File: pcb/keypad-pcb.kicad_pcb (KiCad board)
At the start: 2 copper layers, 38.1 x 59.9 mm, 20 parts, among them SW1 SW_Push, U1 ATmega32U4-A, Y1 Crystal_GND24_Small

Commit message: finalized pcb and created gerbers
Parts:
- moved R3 3.49 mm to (71.1, 88.4)
- moved USB1 3.49 mm to (59.5, 86.6)
- moved R2 2.86 mm to (71.1, 86.0)
- moved SW1 2.73 mm to (88.6, 88.6)
- moved F1 2.20 mm to (76.3, 92.1)
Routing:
- net GND: track 137.9 -> 131.7 mm
- net Net-(U1-D+): track 20.9 -> 16.5 mm
- net +5V: track 119.9 -> 123.2 mm, vias 4 -> 5
- net Net-(U1-D-): track 22.2 -> 19.2 mm
- net VCC: track 11.4 -> 12.5 mm
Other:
- board size 38.1 x 59.9 mm -> 38.1 x 56.3 mm

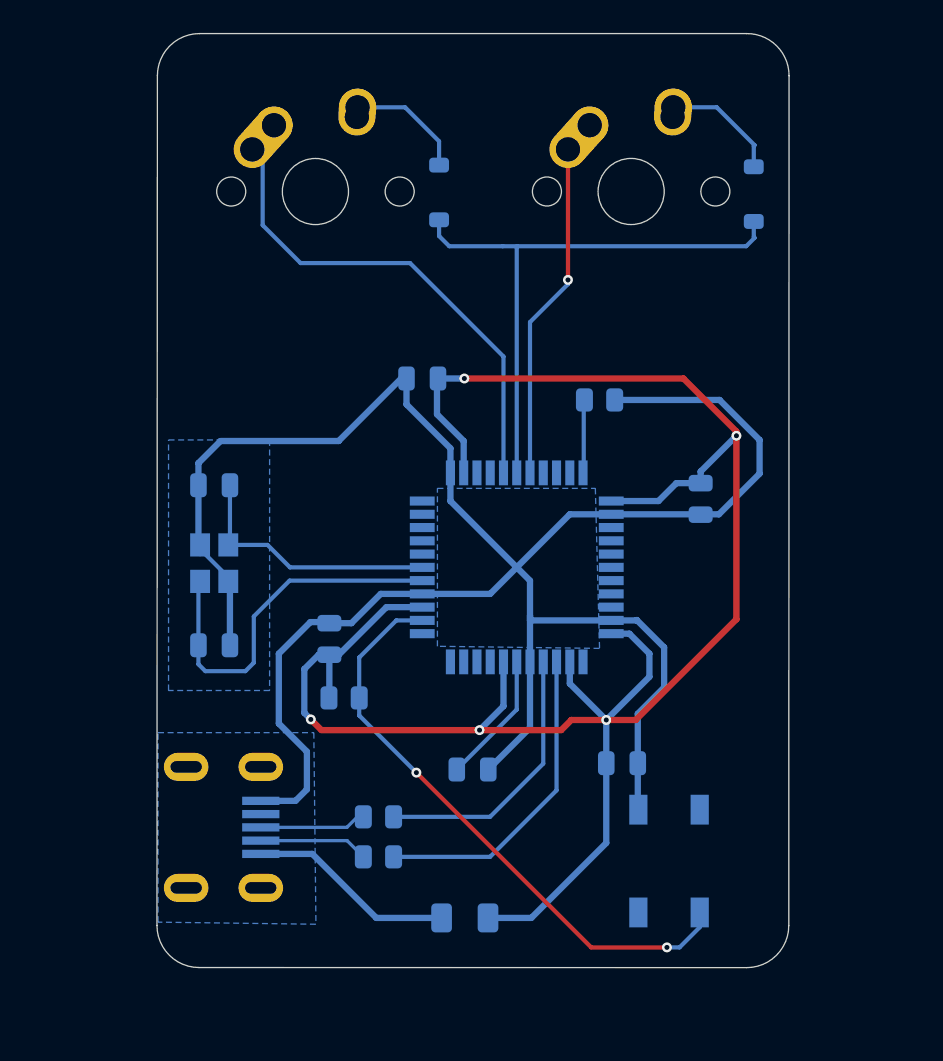
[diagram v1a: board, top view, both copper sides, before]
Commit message: redesigned pcb for front-facing usb
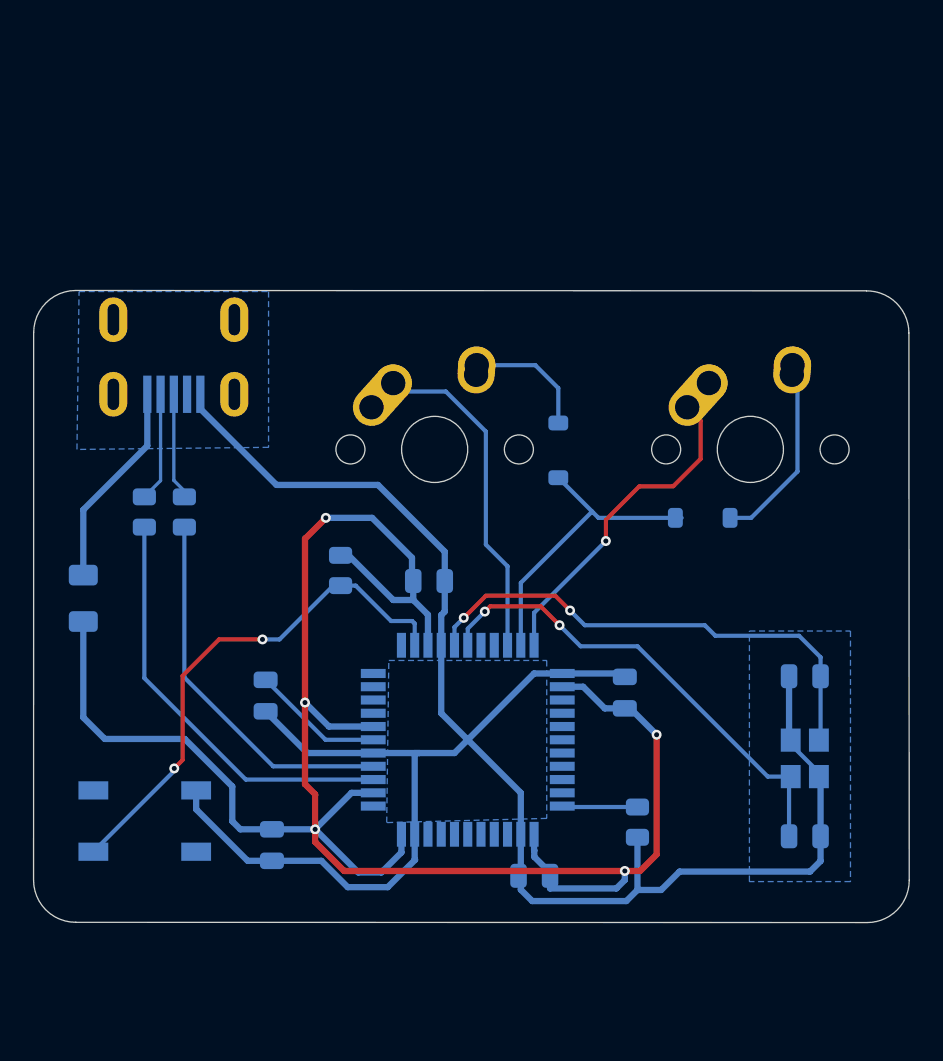
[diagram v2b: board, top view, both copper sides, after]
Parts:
- moved C6 41.4 mm to (96.8, 87.2), turned to 180 degrees
- moved Y1 37.5 mm to (96.8, 82.5), turned to 90 degrees
- moved C7 35.7 mm to (96.8, 77.5), turned to 0 degrees
- moved SW1 31.7 mm to (57.0, 86.2), turned to 0 degrees
- moved USB1 30.6 mm to (58.8, 56.0), turned to -90 degrees
- moved F1 30.0 mm to (53.3, 72.8), turned to -90 degrees
- moved R1 25.6 mm to (86.7, 86.3), turned to -90 degrees
- moved R3 25.1 mm to (57.0, 67.6), turned to -90 degrees
- moved C4 24.8 mm to (80.5, 89.5), turned to 180 degrees
- moved C3 22.5 mm to (86.0, 78.5), turned to 90 degrees
- moved R2 21.8 mm to (59.4, 67.6), turned to 90 degrees
- moved C5 21.7 mm to (64.7, 87.7), turned to -90 degrees
- moved D2 19.8 mm to (90.7, 67.9), turned to 0 degrees
- moved MX1 17.1 mm to (74.5, 63.8)
- moved MX2 17.1 mm to (93.6, 63.8)
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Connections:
- U1 pad 20: unconnected-(U1-PD2-Pad20) -> COL0
- U1 pad 21: unconnected-(U1-PD3-Pad21) -> ROW0
- U1 pad 22: unconnected-(U1-PD5-Pad22) -> COL1
- U1 pad 27: COL0 -> unconnected-(U1-PD7-Pad27)
- U1 pad 28: ROW0 -> unconnected-(U1-PB4-Pad28)
- U1 pad 29: COL1 -> unconnected-(U1-PB5-Pad29)
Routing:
- net ROW0: track 35.2 -> 18.3 mm
- net Net-(U1-XTAL1): track 16.0 -> 29.1 mm, vias 0 -> 2
- net COL0: track 29.7 -> 21.7 mm
- net Net-(U1-XTAL2): track 22.8 -> 30.7 mm, vias 0 -> 2
- net GND: track 131.7 -> 125.3 mm
- net Net-(U1-D-): track 19.2 -> 25.4 mm
- net Net-(U1-D+): track 16.5 -> 22.7 mm
- net Net-(U1-~{RESET}): track 36.0 -> 31.5 mm
- net Net-(D2-A): track 7.60 -> 11.9 mm
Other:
- board size 38.1 x 56.3 mm -> 52.8 x 38.1 mm

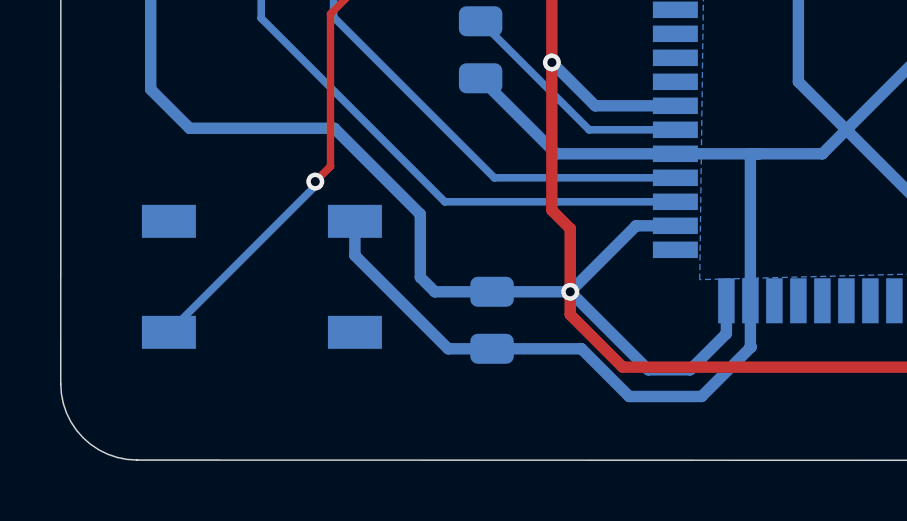
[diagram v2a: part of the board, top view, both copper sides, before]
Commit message: added silkscreened name and serial number and regenerated gerbers
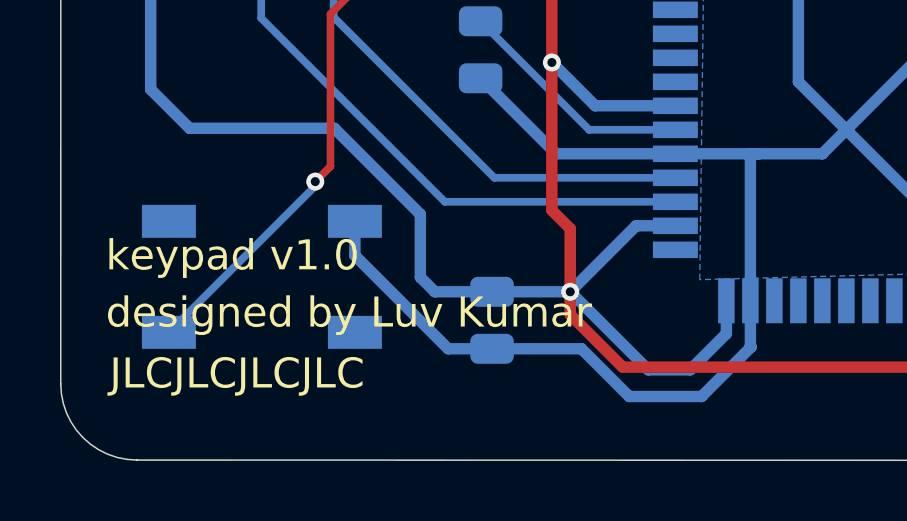
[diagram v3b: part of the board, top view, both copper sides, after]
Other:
- board text added: "JLCJLCJLCJLC"
- board text added: "designed by Luv Kumar"
- board text added: "keypad v1.0"
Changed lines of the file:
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@@
 		(at 74.509 63.817)
 		(property "Reference" "MX1"
-			(at 0 3.175 360)
+			(at 0 3.175 0)
 			(layer "Dwgs.User")
 			(effects
@@
 		)
 		(property "Value" "MX-NoLED"
-			(at 0 -7.9375 360)
+			(at 0 -7.9375 0)
 			(layer "Dwgs.User")
 			(effects
@@
 		(at 93.551117 63.814802)
 		(property "Reference" "MX2"
-			(at 0 3.175 360)
+			(at 0 3.175 0)
 			(layer "Dwgs.User")
 			(effects
@@
 		)
 		(property "Value" "MX-NoLED"
-			(at 0 -7.9375 360)
+			(at 0 -7.9375 0)
 			(layer "Dwgs.User")
 			(effects
@@
 		(tags "SOD-123")
 		(property "Reference" "D2"
-			(at -3.778885 -0.030584 360)
+			(at -3.778885 -0.030584 0)
 			(layer "B.SilkS")
 			(effects
@@
 		)
 		(property "Value" "D_Small"
-			(at 0 -2.1 360)
+			(at 0 -2.1 0)
 			(layer "B.Fab")
 			(effects
@@
 		)
 		(fp_text user "${REFERENCE}"
-			(at 0 2 360)
+			(at 0 2 0)
 			(layer "B.Fab")
 			(effects
@@
 		(tags "capacitor")
 		(property "Reference" "C3"
-			(at 0 1.68 270)
+			(at 0 1.68 -90)
 			(layer "B.SilkS")
 			(effects
@@
 		)
 		(property "Value" "0.1uf"
-			(at 0 -1.68 270)
+			(at 0 -1.68 -90)
 			(layer "B.Fab")
 			(effects
@@
 		)
 		(fp_text user "${REFERENCE}"
-			(at 0 0 270)
+			(at 0 0 -90)
 			(layer "B.Fab")
 			(effects
@@
 		(tags "resistor")
 		(property "Reference" "R4"
-			(at -0.127 1.651 270)
+			(at -0.127 1.651 -90)
 			(layer "B.SilkS")
 			(effects
@@
 		)
 		(property "Value" "10k"
-			(at 0 -1.65 270)
+			(at 0 -1.65 -90)
 			(layer "B.Fab")
 			(effects
@@
 		)
 		(fp_text user "${REFERENCE}"
-			(at 0 0 270)
+			(at 0 0 -90)
 			(layer "B.Fab")
 			(effects
@@
 		(tags "QFP 0.8")
 		(property "Reference" "U1"
-			(at 0 7.45 360)
+			(at 0 7.45 0)
 			(layer "B.SilkS")
 			(effects
@@
 		)
 		(property "Value" "ATmega32U4-A"
-			(at 0 -7.45 360)
+			(at 0 -7.45 0)
 			(layer "B.Fab")
 			(effects
@@
 		)
 		(fp_text user "${REFERENCE}"
-			(at 0 0 360)
+			(at 0 0 0)
 			(layer "B.Fab")
 			(effects
@@
 		(tags "SOD-123")
 		(property "Reference" "D1"
-			(at -3.878521 0.027 270)
+			(at -3.878521 0.027 -90)
 			(layer "B.SilkS")
 			(effects
@@
 		)
 		(property "Value" "D_Small"
-			(at 0 -2.1 270)
+			(at 0 -2.1 -90)
 			(layer "B.Fab")
 			(effects
@@
 		)
 		(fp_text user "${REFERENCE}"
-			(at 0 2 270)
+			(at 0 2 -90)
 			(layer "B.Fab")
 			(effects
@@
 		(tags "SMD SMT crystal")
 		(property "Reference" "Y1"
-			(at 0 -2.67 270)
+			(at 0 -2.67 -90)
 			(layer "B.SilkS")
 			(effects
@@
 		)
 		(property "Value" "Crystal_GND24_Small"
-			(at 0 -2.45 270)
+			(at 0 -2.45 -90)
 			(layer "B.Fab")
 			(effects
@@
 		)
 		(fp_text user "${REFERENCE}"
-			(at 0 0 270)
+			(at 0 0 -90)
 			(layer "B.Fab")
 			(effects
@@
 		(tags "resistor")
 		(property "Reference" "R2"
-			(at -0.1505 1.904 270)
+			(at -0.1505 1.904 -90)
 			(layer "B.SilkS")
 			(effects
@@
 		)
 		(property "Value" "22"
-			(at 0 -1.65 270)
+			(at 0 -1.65 -90)
 			(layer "B.Fab")
 			(effects
@@
 		)
 		(fp_text user "${REFERENCE}"
-			(at 0 0 270)
+			(at 0 0 -90)
 			(layer "B.Fab")
 			(effects
@@
 		(tags "capacitor")
 		(property "Reference" "C7"
-			(at -0.003 -1.967 360)
+			(at -0.003 -1.967 0)
 			(layer "B.SilkS")
 			(effects
@@
 		)
 		(property "Value" "22pf"
-			(at 0 -1.68 360)
+			(at 0 -1.68 0)
 			(layer "B.Fab")
 			(effects
@@
 		)
 		(fp_text user "${REFERENCE}"
-			(at 0 0 360)
+			(at 0 0 0)
 			(layer "B.Fab")
 			(effects
@@
 		(at 57.023 86.233)
 		(property "Reference" "SW1"
-			(at 0 -4.064 360)
+			(at 0 -4.064 0)
 			(layer "B.SilkS")
 			(effects
@@
 		)
 		(property "Value" "SW_Push"
-			(at 0 4.064 360)
+			(at 0 4.064 0)
 			(layer "B.Fab")
 			(effects
@@
 		(tags "capacitor")
 		(property "Reference" "C2"
-			(at 0 1.68 360)
+			(at 0 1.68 0)
 			(layer "B.SilkS")
 			(effects
@@
 		)
 		(property "Value" "0.1uf"
-			(at 0 -1.68 360)
+			(at 0 -1.68 0)
 			(layer "B.Fab")
 			(effects
@@
 		)
 		(fp_text user "${REFERENCE}"
-			(at 0 0 360)
+			(at 0 0 0)
 			(layer "B.Fab")
 			(effects
@@
 		(layer "Edge.Cuts")
 	)
+	(gr_text "JLCJLCJLCJLC"
+		(at 51.943 90.043 -0)
+		(layer "F.SilkS")
+		(effects
+			(font
+				(size 1 1)
+				(thickness 0.1)
+			)
+			(justify left bottom)
+		)
+	)
+	(gr_text "keypad v1.0"
+		(at 51.816 86.106 -0)
+		(layer "F.SilkS")
+		(effects
+			(font
+				(size 1 1)
+				(thickness 0.1)
+			)
+			(justify left bottom)
+		)
+	)
+	(gr_text "designed by Luv Kumar"
+		(at 51.816 88.011 -0)
+		(layer "F.SilkS")
+		(effects
+			(font
+				(size 1 1)
+				(thickness 0.1)
+			)
+			(justify left bottom)
+		)
+	)
 	(segment
